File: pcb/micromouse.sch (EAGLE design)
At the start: 33 parts, among them J1 ENCODER_POLOLU, J2 ENCODER_POLOLU, Q1 PFET, Q2 MOSFET-NCHANNELBSS123LT1G, U1 DRV8833PWP, U2 LD1117, U3 LM3480IM4

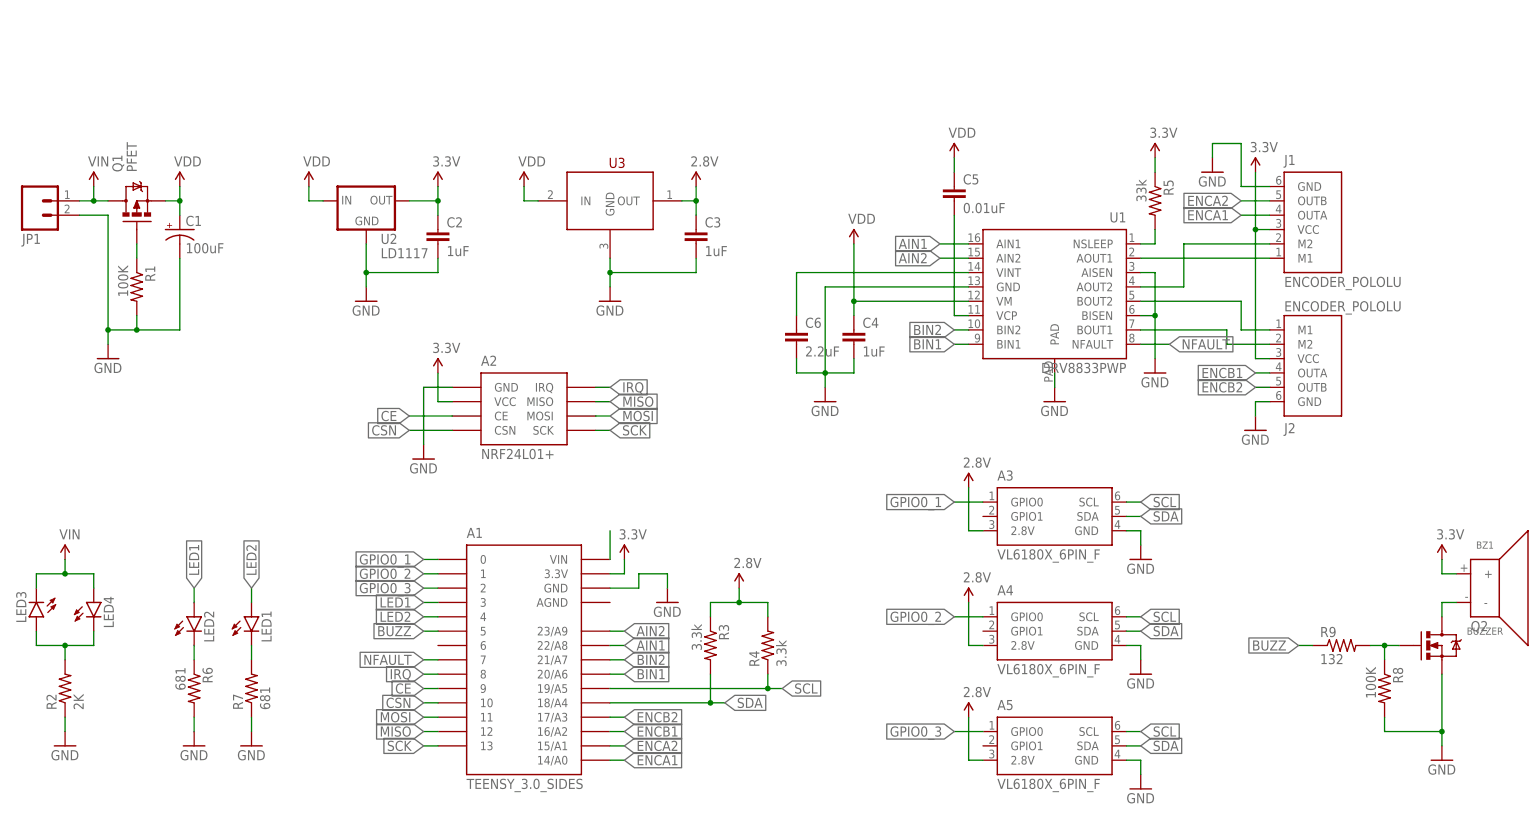
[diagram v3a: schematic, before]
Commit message: Fixed 2.8v regulator pinout
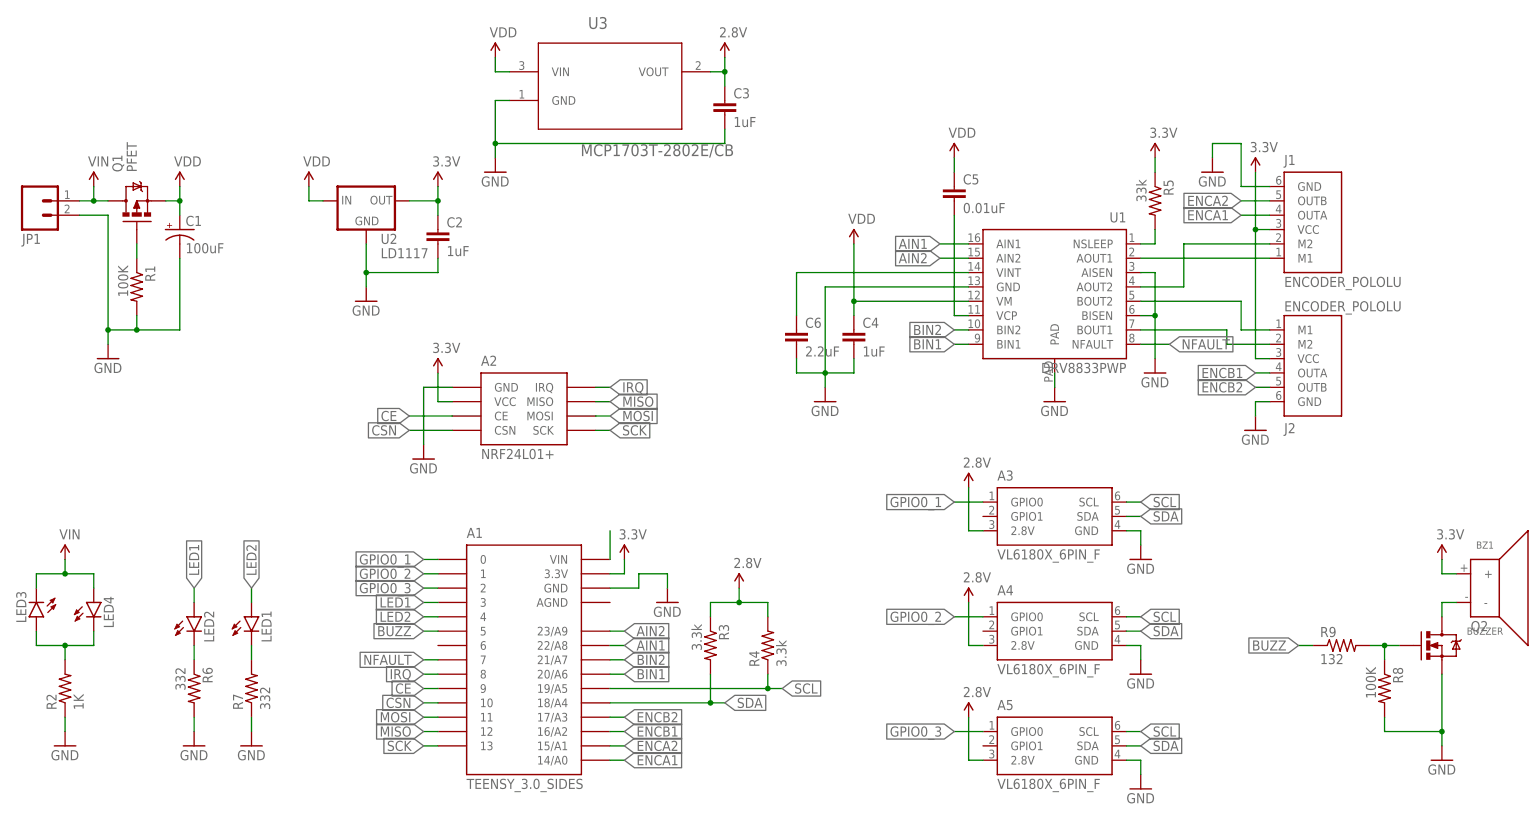
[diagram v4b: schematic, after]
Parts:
- R2: value 2K -> 1K
- R6, R7: value 681 -> 332
- U3: value LM3480IM4 -> MCP1703T-2802E/CB; device SparkFun-PowerIC:LM3480IM4 -> Microchip_By_element14_Batch_1:MCP1703T-3002E/CB
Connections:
- net 2.8V: now also U3.VOUT; no longer U3.OUT
- net VDD: now also U3.VIN; no longer U3.IN
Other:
- moved on the sheet: C3
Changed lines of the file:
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@@
 <part name="U2" library="Custom" deviceset="LD1117" device=""/>
 <part name="A2" library="Custom" deviceset="NRF24L01+" device=""/>
-<part name="U3" library="SparkFun-PowerIC" deviceset="LM3480IM4" device="" value=""/>
 <part name="JP1" library="SparkFun-Connectors" deviceset="M02" device="LOCK_LONGPADS" value=""/>
 <part name="J1" library="Custom" deviceset="ENCODER_POLOLU" device=""/>
@@
 <part name="SUPPLY3" library="SparkFun-Aesthetics" deviceset="VIN" device=""/>
 <part name="SUPPLY4" library="SparkFun-Aesthetics" deviceset="VIN" device=""/>
-<part name="R2" library="SparkFun-Resistors" deviceset="RESISTOR" device="0603" value="2K"/>
+<part name="R2" library="SparkFun-Resistors" deviceset="RESISTOR" device="0603" value="1K"/>
 <part name="GND2" library="SparkFun-Aesthetics" deviceset="GND" device=""/>
 <part name="SUPPLY6" library="SparkFun-Aesthetics" deviceset="VDD" device=""/>
@@
 <part name="SUPPLY18" library="SparkFun-Aesthetics" deviceset="2.8V" device=""/>
 <part name="LED2" library="SparkFun-LED" deviceset="LED" device="0603"/>
-<part name="R6" library="SparkFun-Resistors" deviceset="RESISTOR" device="0603" value="681"/>
+<part name="R6" library="SparkFun-Resistors" deviceset="RESISTOR" device="0603" value="332"/>
 <part name="GND5" library="SparkFun-Aesthetics" deviceset="GND" device=""/>
 <part name="LED1" library="SparkFun-LED" deviceset="LED" device="0603"/>
-<part name="R7" library="SparkFun-Resistors" deviceset="RESISTOR" device="0603" value="681"/>
+<part name="R7" library="SparkFun-Resistors" deviceset="RESISTOR" device="0603" value="332"/>
 <part name="GND16" library="SparkFun-Aesthetics" deviceset="GND" device=""/>
 <part name="C4" library="SparkFun-Capacitors" deviceset="CAP" device="0603-CAP" value="1uF"/>
@@
 <part name="R8" library="SparkFun-Resistors" deviceset="RESISTOR" device="0603" value="100K"/>
 <part name="R9" library="SparkFun-Resistors" deviceset="RESISTOR" device="0603" value="132"/>
+<part name="U3" library="Microchip_By_element14_Batch_1" deviceset="MCP1703T-3002E/CB" device="" value="MCP1703T-2802E/CB"/>
 </parts>
 <sheets>
@@
 <instance part="U2" gate="G$1" x="63.5" y="106.68"/>
 <instance part="A2" gate="G$1" x="91.44" y="68.58"/>
-<instance part="U3" gate="G$1" x="106.68" y="106.68"/>
 <instance part="JP1" gate="G$1" x="5.08" y="106.68" rot="MR180"/>
 <instance part="J1" gate="G$1" x="231.14" y="101.6"/>
@@
 <instance part="LED4" gate="G$1" x="15.24" y="35.56"/>
 <instance part="R1" gate="G$1" x="22.86" y="91.44" rot="R270"/>
-<instance part="C3" gate="G$1" x="121.92" y="99.06"/>
+<instance part="C3" gate="G$1" x="127" y="121.92"/>
 <instance part="C1" gate="G$1" x="30.48" y="101.6"/>
-<instance part="SUPPLY1" gate="G$1" x="121.92" y="109.22"/>
+<instance part="SUPPLY1" gate="G$1" x="127" y="132.08"/>
 <instance part="SUPPLY2" gate="G$1" x="76.2" y="109.22"/>
 <instance part="GND1" gate="1" x="17.78" y="78.74"/>
@@
 <instance part="SUPPLY7" gate="VDD" x="53.34" y="109.22"/>
 <instance part="GND3" gate="1" x="63.5" y="88.9"/>
-<instance part="GND4" gate="1" x="106.68" y="88.9"/>
-<instance part="SUPPLY8" gate="VDD" x="91.44" y="109.22"/>
+<instance part="GND4" gate="1" x="86.36" y="111.76"/>
+<instance part="SUPPLY8" gate="VDD" x="86.36" y="132.08"/>
 <instance part="C2" gate="G$1" x="76.2" y="99.06"/>
 <instance part="LED3" gate="G$1" x="5.08" y="33.02" rot="R180"/>
@@
 <instance part="R8" gate="G$1" x="243.84" y="20.32" rot="R270"/>
 <instance part="R9" gate="G$1" x="236.22" y="27.94"/>
+<instance part="U3" gate="A" x="106.68" y="129.54"/>
 </instances>
 <busses>
@@
 </segment>
 <segment>
-<pinref part="U3" gate="G$1" pin="GND"/>
-<wire x1="106.68" y1="96.52" x2="106.68" y2="93.98" width="0.1524" layer="91"/>
-<wire x1="106.68" y1="93.98" x2="121.92" y2="93.98" width="0.1524" layer="91"/>
-<wire x1="106.68" y1="93.98" x2="106.68" y2="91.44" width="0.1524" layer="91"/>
-<junction x="106.68" y="93.98"/>
+<wire x1="86.36" y1="124.46" x2="86.36" y2="116.84" width="0.1524" layer="91"/>
+<wire x1="86.36" y1="116.84" x2="127" y2="116.84" width="0.1524" layer="91"/>
+<wire x1="86.36" y1="116.84" x2="86.36" y2="114.3" width="0.1524" layer="91"/>
+<junction x="86.36" y="116.84"/>
 <pinref part="C3" gate="G$1" pin="2"/>
-<wire x1="121.92" y1="96.52" x2="121.92" y2="93.98" width="0.1524" layer="91"/>
+<wire x1="127" y1="119.38" x2="127" y2="116.84" width="0.1524" layer="91"/>
 <pinref part="GND4" gate="1" pin="GND"/>
+<pinref part="U3" gate="A" pin="GND"/>
+<wire x1="88.9" y1="124.46" x2="86.36" y2="124.46" width="0.1524" layer="91"/>
 </segment>
 <segment>
@@
 <segment>
 <pinref part="SUPPLY8" gate="VDD" pin="VDD"/>
-<wire x1="91.44" y1="109.22" x2="91.44" y2="106.68" width="0.1524" layer="91"/>
-<pinref part="U3" gate="G$1" pin="IN"/>
-<wire x1="91.44" y1="106.68" x2="93.98" y2="106.68" width="0.1524" layer="91"/>
+<wire x1="86.36" y1="132.08" x2="86.36" y2="129.54" width="0.1524" layer="91"/>
+<wire x1="86.36" y1="129.54" x2="88.9" y2="129.54" width="0.1524" layer="91"/>
+<pinref part="U3" gate="A" pin="VIN"/>
 </segment>
 <segment>
@@
 <segment>
 <pinref part="SUPPLY1" gate="G$1" pin="2.8V"/>
-<wire x1="121.92" y1="109.22" x2="121.92" y2="106.68" width="0.1524" layer="91"/>
-<pinref part="U3" gate="G$1" pin="OUT"/>
-<wire x1="119.38" y1="106.68" x2="121.92" y2="106.68" width="0.1524" layer="91"/>
+<wire x1="127" y1="132.08" x2="127" y2="129.54" width="0.1524" layer="91"/>
+<wire x1="124.46" y1="129.54" x2="127" y2="129.54" width="0.1524" layer="91"/>
 <pinref part="C3" gate="G$1" pin="1"/>
-<wire x1="121.92" y1="106.68" x2="121.92" y2="104.14" width="0.1524" layer="91"/>
-<junction x="121.92" y="106.68"/>
-</segment>
-<segment>
+<wire x1="127" y1="129.54" x2="127" y2="127" width="0.1524" layer="91"/>
+<junction x="127" y="129.54"/>
+<pinref part="U3" gate="A" pin="VOUT"/>
+</segment>
+<segment>

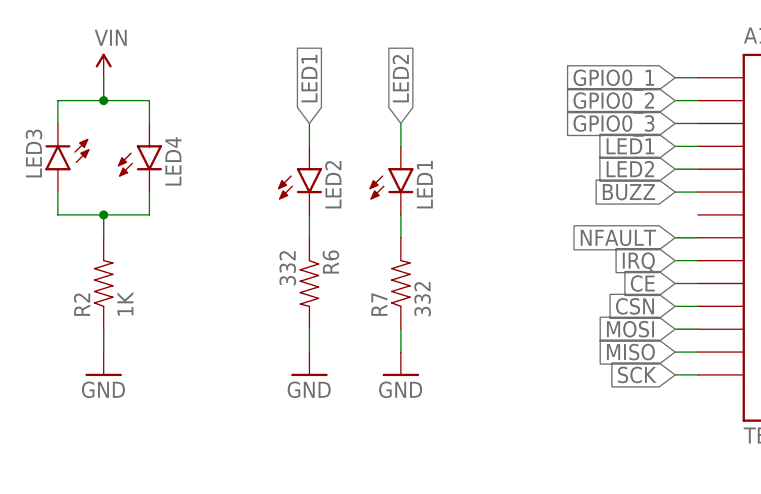
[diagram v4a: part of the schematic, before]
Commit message: Changed led resistors
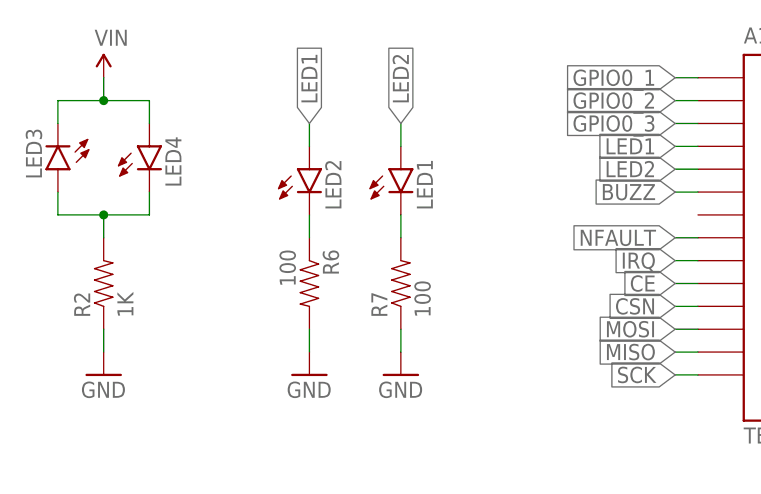
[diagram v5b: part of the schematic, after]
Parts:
- R6, R7: value 332 -> 100
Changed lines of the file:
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@@
 <part name="SUPPLY18" library="SparkFun-Aesthetics" deviceset="2.8V" device=""/>
 <part name="LED2" library="SparkFun-LED" deviceset="LED" device="0603"/>
-<part name="R6" library="SparkFun-Resistors" deviceset="RESISTOR" device="0603" value="332"/>
+<part name="R6" library="SparkFun-Resistors" deviceset="RESISTOR" device="0603" value="100"/>
 <part name="GND5" library="SparkFun-Aesthetics" deviceset="GND" device=""/>
 <part name="LED1" library="SparkFun-LED" deviceset="LED" device="0603"/>
-<part name="R7" library="SparkFun-Resistors" deviceset="RESISTOR" device="0603" value="332"/>
+<part name="R7" library="SparkFun-Resistors" deviceset="RESISTOR" device="0603" value="100"/>
 <part name="GND16" library="SparkFun-Aesthetics" deviceset="GND" device=""/>
 <part name="C4" library="SparkFun-Capacitors" deviceset="CAP" device="0603-CAP" value="1uF"/>

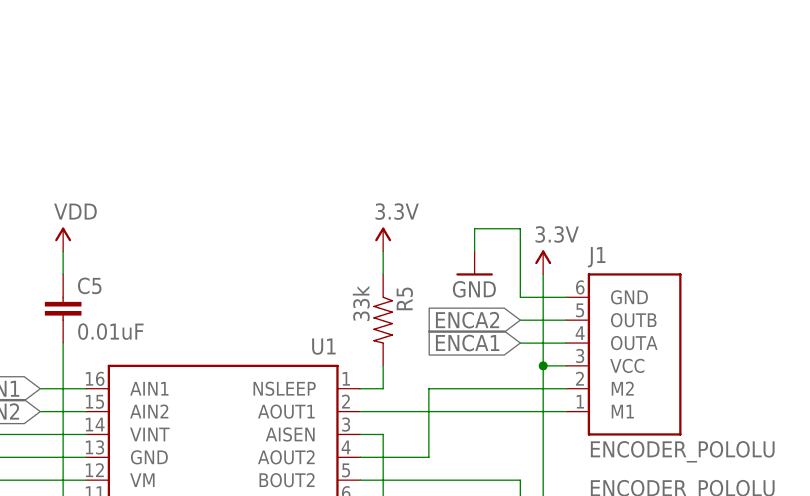
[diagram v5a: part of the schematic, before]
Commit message: Fixed nsleep signal on board
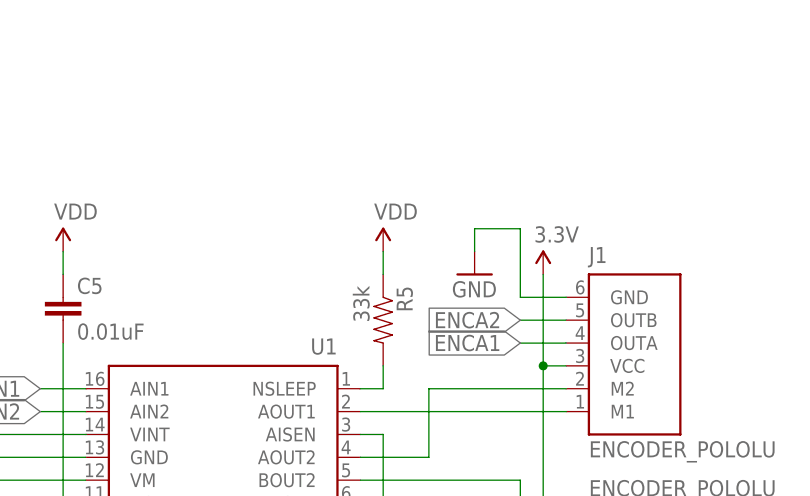
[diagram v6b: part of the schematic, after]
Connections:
- net 3.3V: no longer R5.1
- net VDD: now also R5.1
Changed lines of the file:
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@@
 <part name="SUPPLY10" library="SparkFun-Aesthetics" deviceset="3.3V" device=""/>
 <part name="R5" library="SparkFun-Resistors" deviceset="RESISTOR" device="0603" value="33k"/>
-<part name="SUPPLY11" library="SparkFun-Aesthetics" deviceset="3.3V" device=""/>
 <part name="GND9" library="SparkFun-Aesthetics" deviceset="GND" device=""/>
 <part name="GND10" library="SparkFun-Aesthetics" deviceset="GND" device=""/>
@@
 <part name="R9" library="SparkFun-Resistors" deviceset="RESISTOR" device="0603" value="132"/>
 <part name="U3" library="Microchip_By_element14_Batch_1" deviceset="MCP1703T-3002E/CB" device="" value="MCP1703T-2802E/CB"/>
+<part name="SUPPLY11" library="SparkFun-Aesthetics" deviceset="VDD" device=""/>
 </parts>
 <sheets>
@@
 <instance part="SUPPLY10" gate="G$1" x="220.98" y="111.76"/>
 <instance part="R5" gate="G$1" x="203.2" y="106.68" rot="R270"/>
-<instance part="SUPPLY11" gate="G$1" x="203.2" y="114.3"/>
 <instance part="GND9" gate="1" x="185.42" y="71.12"/>
 <instance part="GND10" gate="1" x="144.78" y="71.12"/>
@@
 <instance part="R9" gate="G$1" x="236.22" y="27.94"/>
 <instance part="U3" gate="A" x="106.68" y="129.54"/>
+<instance part="SUPPLY11" gate="VDD" x="203.2" y="114.3"/>
 </instances>
 <busses>
@@
 <pinref part="C4" gate="G$1" pin="1"/>
 </segment>
+<segment>
+<pinref part="R5" gate="G$1" pin="1"/>
+<wire x1="203.2" y1="114.3" x2="203.2" y2="111.76" width="0.1524" layer="91"/>
+<pinref part="SUPPLY11" gate="VDD" pin="VDD"/>
+</segment>
 </net>
 <net name="3.3V" class="0">
@@
 </segment>
 <segment>
-<pinref part="R5" gate="G$1" pin="1"/>
-<pinref part="SUPPLY11" gate="G$1" pin="3.3V"/>
-<wire x1="203.2" y1="114.3" x2="203.2" y2="111.76" width="0.1524" layer="91"/>
-</segment>
-<segment>
